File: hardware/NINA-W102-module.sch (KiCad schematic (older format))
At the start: 4 parts, among them J6 NINA Module left header, J7 Shield left header, J8 Shield right header, J9 Nina module right header

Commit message: removed duplicated battery terminal
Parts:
- J6, J9: footprint (none) -> Socket_Strips:Socket_Strip_Straight_1x15_Pitch2.54mm
- J7, J8: footprint (none) -> lib:1X15_LOCK
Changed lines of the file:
@@
 Title "IoT conference badge - mainboard"
 Date "2018-05-20"
-Rev "0.3.4"
+Rev "0.3.5"
 Comp "MakeZürich (makezurich.ch) & GDG Zürich (gdgzh.ch)"
 Comment1 ""
@@
 F 0 "J6" H 4500 4250 50  0000 C CNN
 F 1 "NINA Module left header" H 4050 2650 50  0000 C CNN
-F 2 "" H 4500 3450 50  0001 C CNN
+F 2 "Socket_Strips:Socket_Strip_Straight_1x15_Pitch2.54mm" H 4500 3450 50  0001 C CNN
 F 3 "" H 4500 3450 50  0001 C CNN
 	1    4500 3450
@@
 F 0 "J9" H 7100 4250 50  0000 C CNN
 F 1 "Nina module right header" H 6650 2650 50  0000 C CNN
-F 2 "" H 7100 3450 50  0001 C CNN
+F 2 "Socket_Strips:Socket_Strip_Straight_1x15_Pitch2.54mm" H 7100 3450 50  0001 C CNN
 F 3 "" H 7100 3450 50  0001 C CNN
 	1    7100 3450
@@
 F 0 "J7" H 5000 4250 50  0000 C CNN
 F 1 "Shield left header" H 5050 2650 50  0000 C CNN
-F 2 "" H 5000 3450 50  0001 C CNN
+F 2 "lib:1X15_LOCK" H 5000 3450 50  0001 C CNN
 F 3 "" H 5000 3450 50  0001 C CNN
 	1    5000 3450
@@
 F 0 "J8" H 6550 4250 50  0000 C CNN
 F 1 "Shield right header" H 6600 2650 50  0000 C CNN
-F 2 "" H 6550 3450 50  0001 C CNN
+F 2 "lib:1X15_LOCK" H 6550 3450 50  0001 C CNN
 F 3 "" H 6550 3450 50  0001 C CNN
 	1    6550 3450

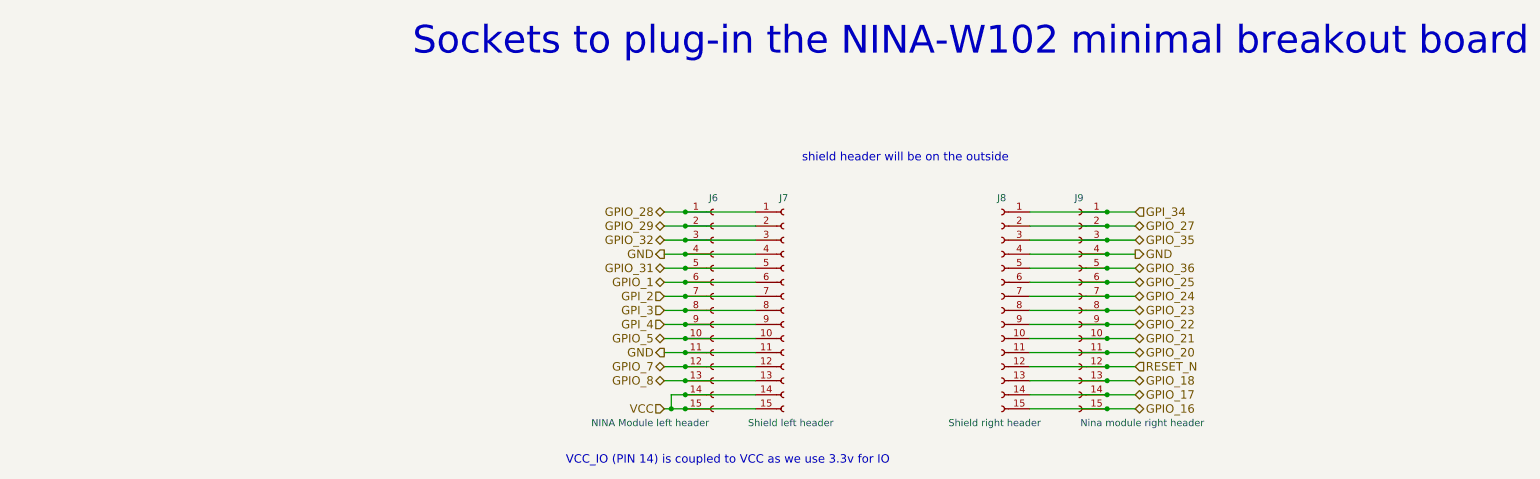
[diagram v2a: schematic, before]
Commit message: Added nina breakout component for footprint matching
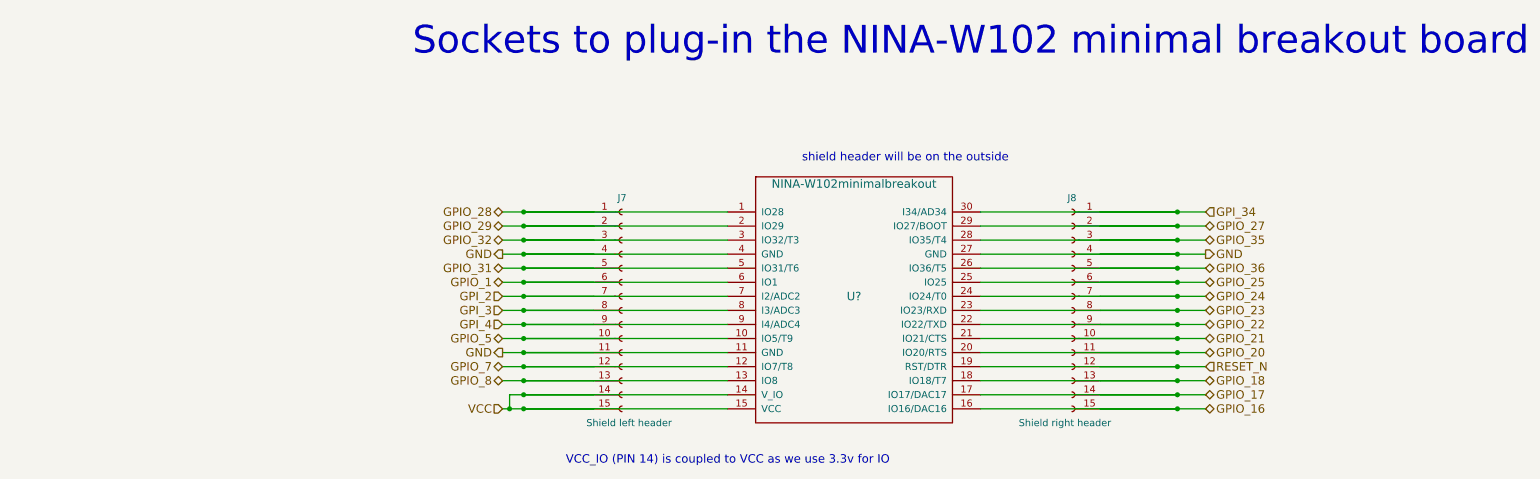
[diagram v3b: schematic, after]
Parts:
- removed J6: NINA Module left header, Socket_Strips:Socket_Strip_Straight_1x15_Pitch2.54mm, symbol Conn_01x15_Female
- removed J9: Nina module right header, Socket_Strips:Socket_Strip_Straight_1x15_Pitch2.54mm, symbol Conn_01x15_Female
- added U?: NINA-W102minimalbreakout, symbol NINA-W102minimalbreakout
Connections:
- net GND: now also U?.11 (GND), U?.27 (GND), U?.4 (GND)
- net GPIO_1: now also U?.6 (IO1)
- net GPIO_16: now also U?.16 (IO16/DAC16)
- net GPIO_17: now also U?.17 (IO17/DAC17)
- net GPIO_18: now also U?.18 (IO18/T7)
- net GPIO_20: now also U?.20 (IO20/RTS)
- net GPIO_21: now also U?.21 (IO21/CTS)
- net GPIO_22: now also U?.22 (IO22/TXD)
- net GPIO_23: now also U?.23 (IO23/RXD)
- net GPIO_24: now also U?.24 (IO24/T0)
- net GPIO_25: now also U?.25 (IO25)
- net GPIO_27: now also U?.29 (IO27/BOOT)
- net GPIO_28: now also U?.1 (IO28)
- net GPIO_29: now also U?.2 (IO29)
- net GPIO_31: now also U?.5 (IO31/T6)
- net GPIO_32: now also U?.3 (IO32/T3)
- net GPIO_35: now also U?.28 (IO35/T4)
- net GPIO_36: now also U?.26 (IO36/T5)
- net GPIO_5: now also U?.10 (IO5/T9)
- net GPIO_7: now also U?.12 (IO7/T8)
- net GPIO_8: now also U?.13 (IO8)
- net GPI_2: now also U?.7 (I2/ADC2)
- net GPI_3: now also U?.8 (I3/ADC3)
- net GPI_34: now also U?.30 (I34/AD34)
- net GPI_4: now also U?.9 (I4/ADC4)
- net RESET_N: now also U?.19 (RST/DTR)
- net VCC: now also U?.14 (V_IO), U?.15 (VCC)
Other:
- moved on the sheet: J7, J8

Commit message: Added footprints for modules
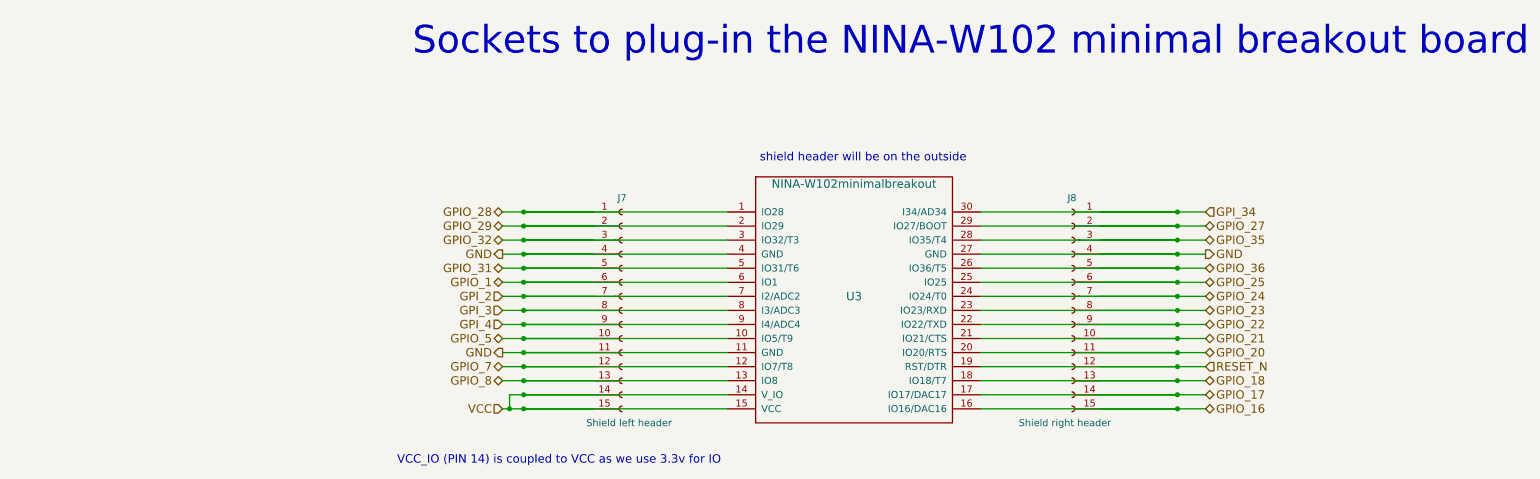
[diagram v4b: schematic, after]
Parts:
- U3: renamed from U?; footprint (none) -> badgeComponents:ublox_NINA-W102_minimal_breakout
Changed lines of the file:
@@
 Text HLabel 3000 4150 0    60   Input ~ 0
 VCC
-Text Notes 3450 4550 0    60   ~ 0
+Text Notes 2250 4550 0    60   ~ 0
 VCC_IO (PIN 14) is coupled to VCC as we use 3.3v for IO
 Text HLabel 8000 2750 2    60   Input ~ 0
@@
 	-1   0    0    -1
 $EndComp
-Text Notes 6600 2400 2    60   ~ 0
+Text Notes 6300 2400 2    60   ~ 0
 shield header will be on the outside
 $Comp
-L NINA-W102minimalbreakout U?
+L NINA-W102minimalbreakout U3
 U 1 1 5B03A795
 P 5500 3300
-F 0 "U?" H 5500 3250 60  0000 C CNN
+F 0 "U3" H 5500 3250 60  0000 C CNN
 F 1 "NINA-W102minimalbreakout" H 5500 4050 60  0000 C CNN
-F 2 "" H 5500 2900 60  0001 C CNN
-F 3 "" H 5500 2900 60  0001 C CNN
+F 2 "badgeComponents:ublox_NINA-W102_minimal_breakout" H 5500 2900 60  0001 C CNN
+F 3 "http://rac.su/ninab" H 5500 2900 60  0001 C CNN
 	1    5500 3300
 	1    0    0    -1

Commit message: Initial netlist import and start of placing components
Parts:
- J7, J8: footprint lib:1X15_LOCK -> badgeComponents:HEADER_1X15_LOCK
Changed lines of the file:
@@
 F 0 "J7" H 3850 4250 50  0000 C CNN
 F 1 "Shield left header" H 3900 2650 50  0000 C CNN
-F 2 "lib:1X15_LOCK" H 3850 3450 50  0001 C CNN
+F 2 "badgeComponents:HEADER_1X15_LOCK" H 3850 3450 50  0001 C CNN
 F 3 "" H 3850 3450 50  0001 C CNN
 	1    3850 3450
@@
 F 0 "J8" H 7050 4250 50  0000 C CNN
 F 1 "Shield right header" H 7100 2650 50  0000 C CNN
-F 2 "lib:1X15_LOCK" H 7050 3450 50  0001 C CNN
+F 2 "badgeComponents:HEADER_1X15_LOCK" H 7050 3450 50  0001 C CNN
 F 3 "" H 7050 3450 50  0001 C CNN
 	1    7050 3450

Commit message: added some more comments
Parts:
- J7, J8: Description (none) -> Leave unpopulated
- U3: Description (none) -> On each side there needs to be a Female header 2.54mm spaci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
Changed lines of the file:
@@
 P 3850 3450
 F 0 "J7" H 3850 4250 50  0000 C CNN
-F 1 "Shield left header" H 3900 2650 50  0000 C CNN
+F 1 "Shield left header" H 3550 2650 50  0000 C CNN
 F 2 "badgeComponents:HEADER_1X15_LOCK" H 3850 3450 50  0001 C CNN
 F 3 "" H 3850 3450 50  0001 C CNN
+F 4 "Leave unpopulated" H 3850 3450 60  0001 C CNN "Description"
 	1    3850 3450
 	1    0    0    -1
@@
 P 7050 3450
 F 0 "J8" H 7050 4250 50  0000 C CNN
-F 1 "Shield right header" H 7100 2650 50  0000 C CNN
+F 1 "Shield right header" H 6550 2650 50  0000 C CNN
 F 2 "badgeComponents:HEADER_1X15_LOCK" H 7050 3450 50  0001 C CNN
 F 3 "" H 7050 3450 50  0001 C CNN
+F 4 "Leave unpopulated" H 7050 3450 60  0001 C CNN "Description"
 	1    7050 3450
 	-1   0    0    -1
@@
 F 2 "badgeComponents:ublox_NINA-W102_minimal_breakout" H 5500 2900 60  0001 C CNN
 F 3 "http://rac.su/ninab" H 5500 2900 60  0001 C CNN
+F 4 "On each side there needs to be a Female header 2.54mm spacing. This is the place where the NINA module will be plugged in" H 5500 3300 60  0001 C CNN "Description"
 	1    5500 3300
 	1    0    0    -1
